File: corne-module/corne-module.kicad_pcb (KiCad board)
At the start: 2 copper layers, 16.6 x 10.7 mm, 7 parts, among them J1 Battery Connector, J2 nice!view, J3 USB_C_Receptacle_PowerOnly_6P, J4 Battery Wire, U1 ProMicro

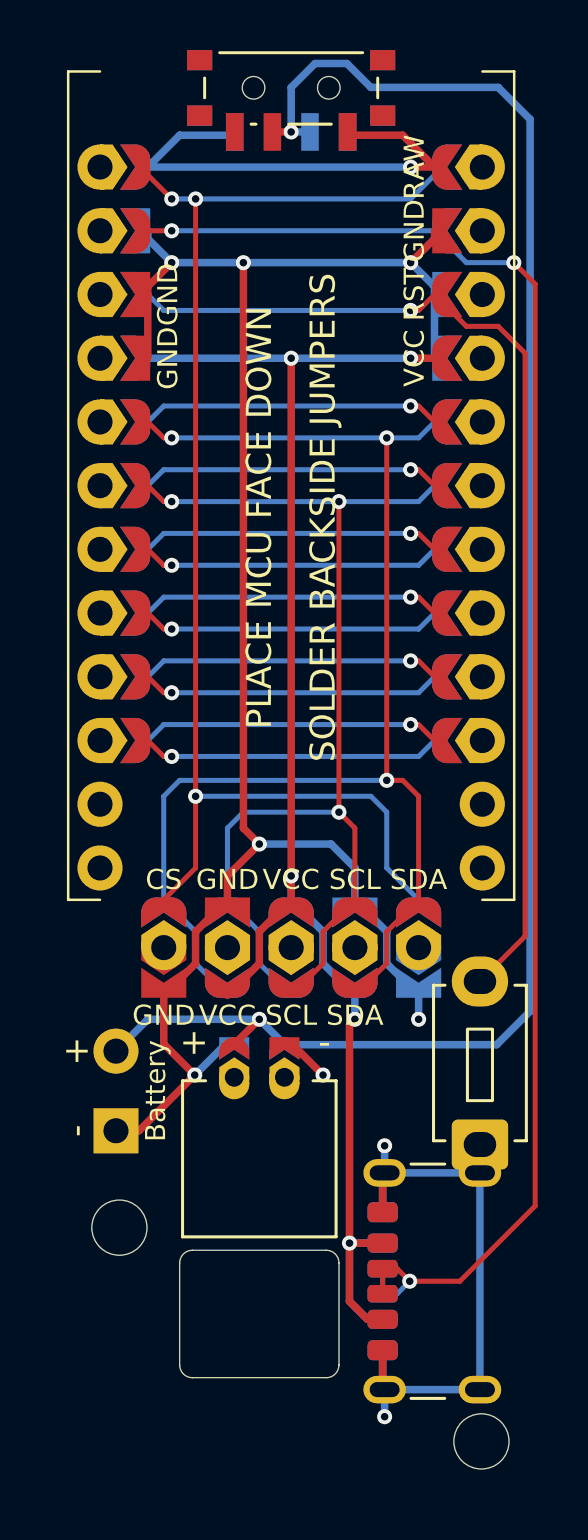
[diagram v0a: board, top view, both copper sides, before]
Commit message: instruction and battery jst hole update
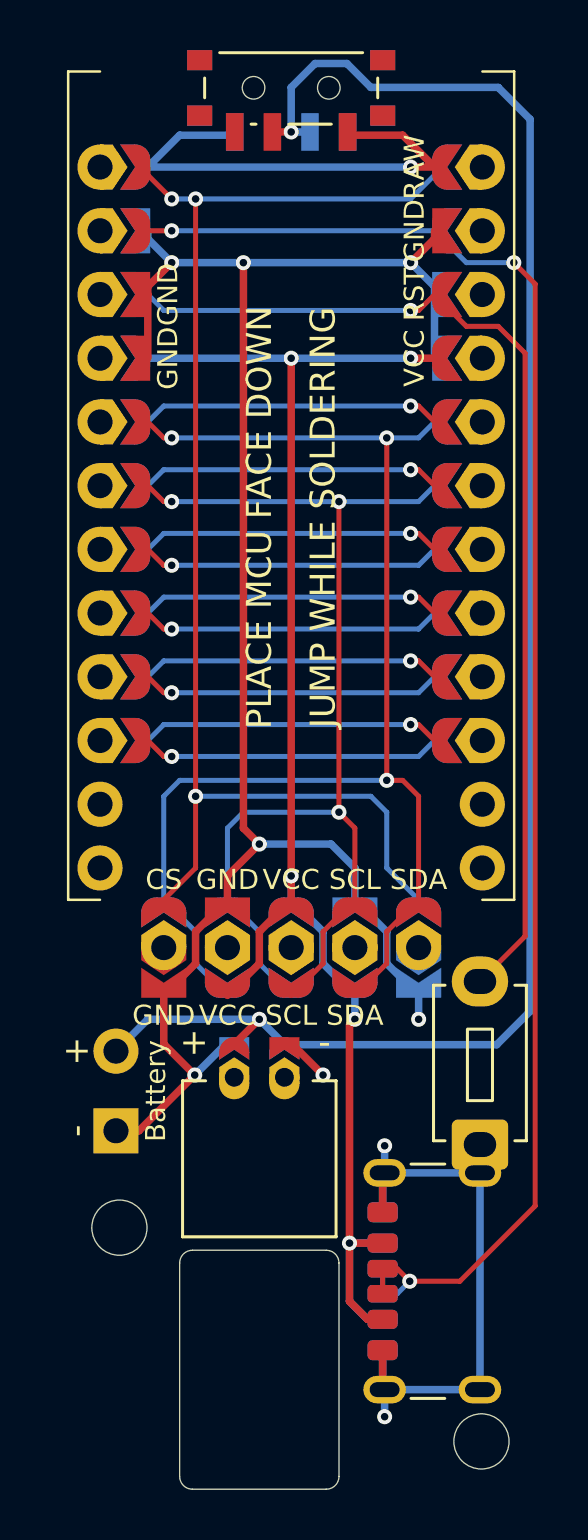
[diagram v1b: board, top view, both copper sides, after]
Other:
- board size 16.6 x 10.7 mm -> 16.6 x 11.5 mm
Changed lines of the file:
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@@
 		(pad_to_mask_clearance 0)
 		(allow_soldermask_bridges_in_footprints no)
-		(grid_origin 164.625 77.195)
+		(grid_origin 164.625 41)
 		(pcbplotparams
 			(layerselection 0x00010fc_ffffffff)
@@
 			(layer "F.Fab")
 		)
-		(fp_text user "SOLDER BACKSIDE JUMPERS"
-			(at -1.27 0 -90)
+		(fp_text user "GND"
+			(at -4.445 -11.43 -90)
 			(unlocked yes)
 			(layer "B.SilkS")
 			(effects
 				(font
-					(size 1 1)
-					(thickness 0.15)
+					(size 0.8 0.8)
+					(thickness 0.1)
 				)
-				(justify mirror)
+				(justify top mirror)
 			)
 		)
-		(fp_text user "GND"
-			(at 4.445 -8.89 -90)
+		(fp_text user "RST"
+			(at -4.445 -8.89 -90)
 			(unlocked yes)
 			(layer "B.SilkS")
@@
 					(thickness 0.1)
 				)
-				(justify bottom mirror)
+				(justify top mirror)
 			)
 		)
@@
 		)
 		(fp_text user "GND"
-			(at -4.445 -11.43 -90)
+			(at 4.445 -6.35 -90)
 			(unlocked yes)
 			(layer "B.SilkS")
@@
 					(thickness 0.1)
 				)
-				(justify top mirror)
+				(justify bottom mirror)
 			)
 		)
-		(fp_text user "VCC"
-			(at -4.445 -6.35 -90)
+		(fp_text user "RAW"
+			(at -4.445 -13.97 -90)
 			(unlocked yes)
 			(layer "B.SilkS")
@@
 			)
 		)
-		(fp_text user "RAW"
-			(at -4.445 -13.97 -90)
+		(fp_text user "VCC"
+			(at -4.445 -6.35 -90)
 			(unlocked yes)
 			(layer "B.SilkS")
@@
 			)
 		)
-		(fp_text user "GND"
-			(at 4.445 -6.35 -90)
+		(fp_text user "JUMP WHILE SOLDERING"
+			(at -1.27 0 -90)
 			(unlocked yes)
 			(layer "B.SilkS")
 			(effects
 				(font
-					(size 0.8 0.8)
-					(thickness 0.1)
+					(size 1 1)
+					(thickness 0.15)
 				)
-				(justify bottom mirror)
+				(justify mirror)
 			)
 		)
-		(fp_text user "RST"
-			(at -4.445 -8.89 -90)
+		(fp_text user "GND"
+			(at 4.445 -8.89 -90)
 			(unlocked yes)
 			(layer "B.SilkS")
@@
 					(thickness 0.1)
 				)
-				(justify top mirror)
+				(justify bottom mirror)
 			)
 		)
-		(fp_text user "GND"
-			(at -4.445 -8.89 90)
+		(fp_text user "JUMP WHILE SOLDERING"
+			(at 1.27 0 90)
 			(unlocked yes)
 			(layer "F.SilkS")
 			(effects
 				(font
-					(size 0.8 0.8)
-					(thickness 0.1)
+					(size 1 1)
+					(thickness 0.15)
 				)
-				(justify bottom)
 			)
 		)
-		(fp_text user "RAW"
-			(at 4.445 -13.97 90)
+		(fp_text user "PLACE MCU FACE DOWN"
+			(at -1.27 0 90)
 			(unlocked yes)
 			(layer "F.SilkS")
 			(effects
 				(font
-					(size 0.8 0.8)
-					(thickness 0.1)
+					(size 1 1)
+					(thickness 0.15)
 				)
-				(justify top)
 			)
 		)
-		(fp_text user "VCC"
-			(at 4.445 -6.35 90)
+		(fp_text user "GND"
+			(at 4.445 -11.43 90)
 			(unlocked yes)
 			(layer "F.SilkS")
@@
 			)
 		)
-		(fp_text user "SOLDER BACKSIDE JUMPERS"
-			(at 1.27 0 90)
+		(fp_text user "GND"
+			(at -4.445 -6.35 90)
 			(unlocked yes)
 			(layer "F.SilkS")
 			(effects
 				(font
-					(size 1 1)
-					(thickness 0.15)
+					(size 0.8 0.8)
+					(thickness 0.1)
 				)
+				(justify bottom)
 			)
 		)
-		(fp_text user "PLACE MCU FACE DOWN"
-			(at -1.27 0 90)
+		(fp_text user "RAW"
+			(at 4.445 -13.97 90)
 			(unlocked yes)
 			(layer "F.SilkS")
 			(effects
 				(font
-					(size 1 1)
-					(thickness 0.15)
+					(size 0.8 0.8)
+					(thickness 0.1)
 				)
+				(justify top)
 			)
 		)
-		(fp_text user "RST"
-			(at 4.445 -8.89 90)
+		(fp_text user "GND"
+			(at -4.445 -8.89 90)
 			(unlocked yes)
 			(layer "F.SilkS")
@@
 					(thickness 0.1)
 				)
-				(justify top)
+				(justify bottom)
 			)
 		)
-		(fp_text user "GND"
-			(at 4.445 -11.43 90)
+		(fp_text user "RST"
+			(at 4.445 -8.89 90)
 			(unlocked yes)
 			(layer "F.SilkS")
@@
 			)
 		)
-		(fp_text user "GND"
-			(at -4.445 -6.35 90)
+		(fp_text user "VCC"
+			(at 4.445 -6.35 90)
 			(unlocked yes)
 			(layer "F.SilkS")
@@
 					(thickness 0.1)
 				)
-				(justify bottom)
+				(justify top)
 			)
 		)
@@
 	)
 	(gr_line
-		(start 160.18 93.832)
+		(start 160.18 98.277)
 		(end 160.18 89.768)
 		(stroke
@@
 	)
 	(gr_line
-		(start 166.53 93.832)
+		(start 166.53 98.277)
 		(end 166.53 89.768)
 		(stroke
@@
 	)
 	(gr_line
-		(start 160.688 94.34)
-		(end 166.022 94.34)
+		(start 160.688 98.785)
+		(end 166.022 98.785)
 		(stroke
 			(width 0.05)
@@
 	)
 	(gr_arc
-		(start 166.53 93.832)
-		(mid 166.38121 94.19121)
-		(end 166.022 94.34)
+		(start 166.53 98.277)
+		(mid 166.38121 98.63621)
+		(end 166.022 98.785)
 		(stroke
 			(width 0.05)
@@
 	)
 	(gr_arc
-		(start 160.688 94.34)
-		(mid 160.32879 94.19121)
-		(end 160.18 93.832)
+		(start 160.688 98.785)
+		(mid 160.32879 98.63621)
+		(end 160.18 98.277)
 		(stroke
 			(width 0.05)
